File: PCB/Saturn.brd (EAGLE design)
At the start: 58.5 x 61 mm, 21 parts, among them U1A SN74AHCT125N, U2A SN74AHCT125N, U3A SN74AHCT125N, U4A SN74AHCT125N

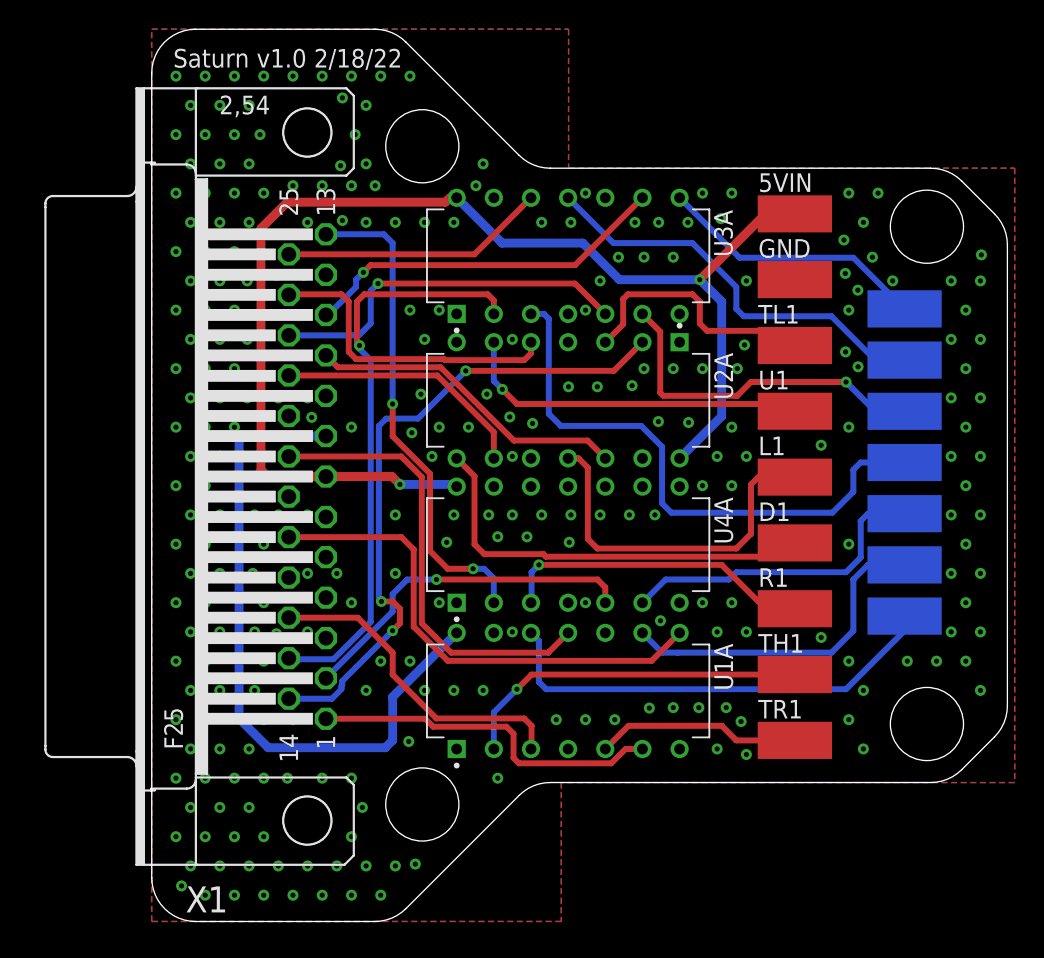
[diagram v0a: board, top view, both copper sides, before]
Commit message: PCB Updates/New Additions
All existing PCBs had silkscreen updates and NES, Virtual Boy, PSX/PS2, Nintendo 64, Saturn have been added.
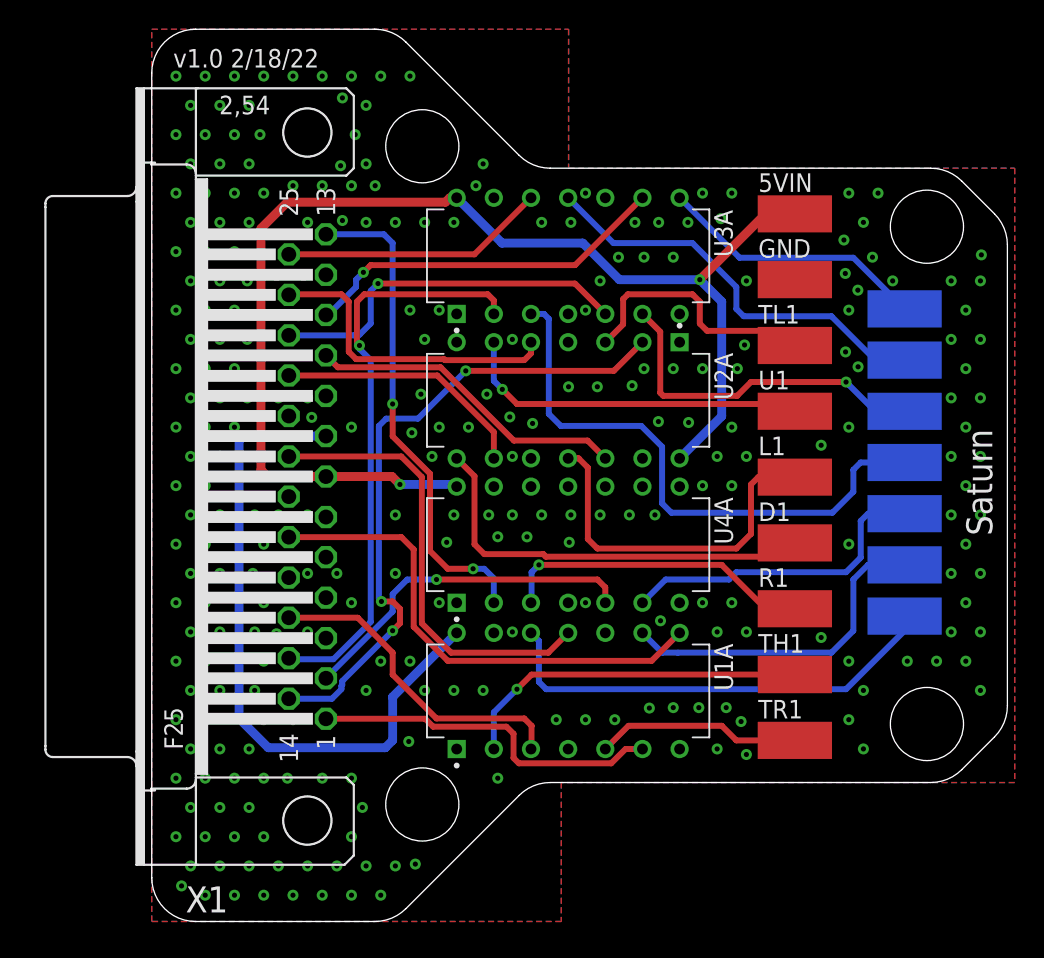
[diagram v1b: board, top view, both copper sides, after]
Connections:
- net NEEDPINID renamed IO16
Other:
- board text added: "Saturn"
- board text added: "v1.0 2/18/22"
- board text removed: "Saturn v1.0 2/18/22"
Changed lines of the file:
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@@
 <drawing>
 <settings>
-<setting alwaysvectorfont="yes"/>
+<setting alwaysvectorfont="no"/>
 <setting verticaltext="up"/>
 </settings>
@@
 <hole x="18.53" y="53.12" drill="5"/>
 <hole x="18.53" y="8.12" drill="5"/>
-<text x="1.5" y="58.5" size="1.27" layer="21">Saturn v1.0 2/18/22</text>
+<text x="1.5" y="58.5" size="1.27" layer="21">v1.0 2/18/22</text>
+<text x="57.5" y="26.5" size="1.778" layer="21" rot="R90">Saturn</text>
 </plain>
 <attributes>
@@
 <wire x1="47.5" y1="16" x2="51.5" y2="20" width="0.4064" layer="16"/>
 </signal>
-<signal name="NEEDPINID">
-<contactref element="U1A" pad="11"/>
-<contactref element="X1" pad="20"/>
-<wire x1="28.5" y1="19.851" x2="27.149" y2="18.5" width="0.4064" layer="1"/>
-<wire x1="27.149" y1="18.5" x2="20.5" y2="18.5" width="0.4064" layer="1"/>
-<wire x1="18.5" y1="20.5" x2="18.5" y2="30.5" width="0.4064" layer="1"/>
-<wire x1="18.5" y1="30.5" x2="17.0884" y2="31.9116" width="0.4064" layer="1"/>
-<wire x1="17.0884" y1="31.9116" x2="9.4" y2="31.9116" width="0.4064" layer="1"/>
-<wire x1="20.5" y1="18.5" x2="18.5" y2="20.5" width="0.4064" layer="1"/>
-</signal>
 <signal name="TL1">
 <contactref element="U2A" pad="3"/>
@@
 <wire x1="35.169" y1="23.5" x2="39.5" y2="23.5" width="0.4064" layer="16"/>
 </signal>
+<signal name="IO16">
+<contactref element="X1" pad="20"/>
+<contactref element="U1A" pad="11"/>
+<wire x1="28.5" y1="19.851" x2="27.149" y2="18.5" width="0.4064" layer="1"/>
+<wire x1="27.149" y1="18.5" x2="20.5" y2="18.5" width="0.4064" layer="1"/>
+<wire x1="18.5" y1="20.5" x2="18.5" y2="30.5" width="0.4064" layer="1"/>
+<wire x1="17.0884" y1="31.9116" x2="18.5" y2="30.5" width="0.4064" layer="1"/>
+<wire x1="20.5" y1="18.5" x2="18.5" y2="20.5" width="0.4064" layer="1"/>
+<wire x1="9.4" y1="31.9116" x2="17.0884" y2="31.9116" width="0.4064" layer="1"/>
+</signal>
 </signals>

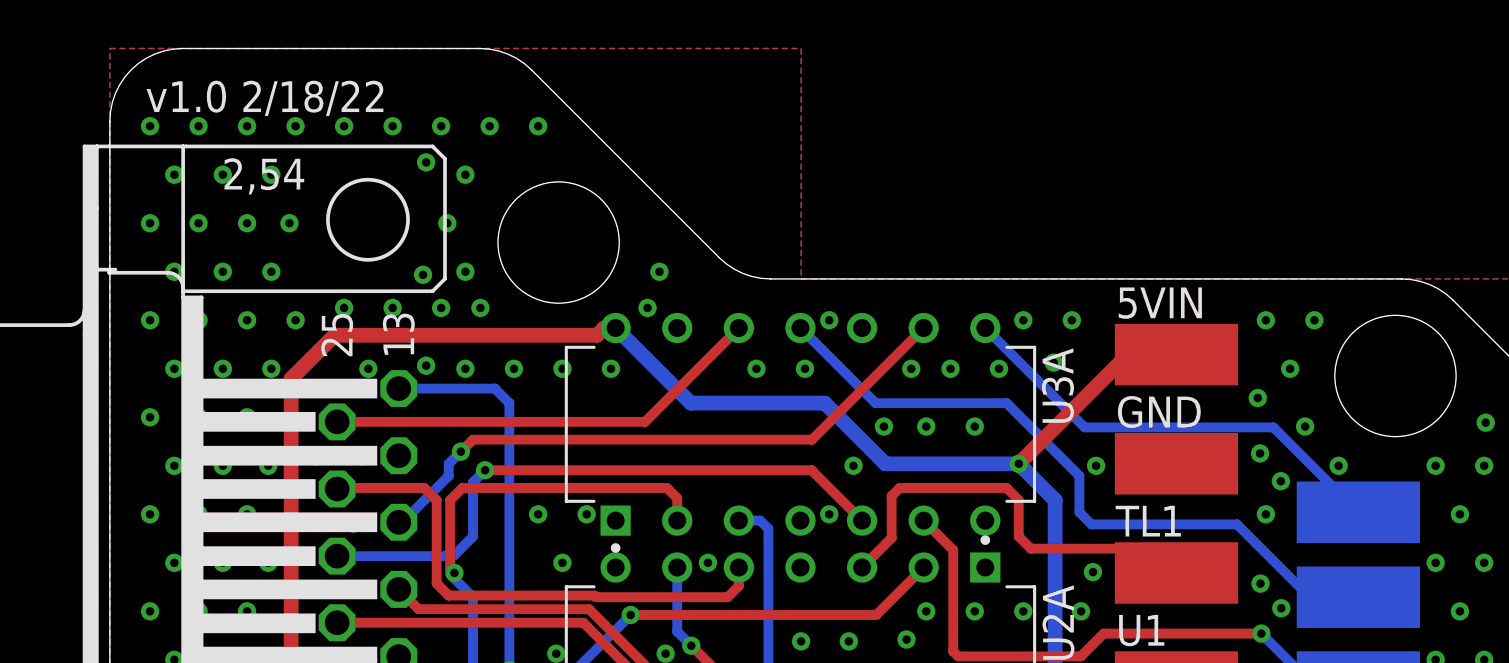
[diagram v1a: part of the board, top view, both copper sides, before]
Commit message: Datasheets, BOM Update, 3 New PCBs
Added Datasheets for the Female/Male DB25 connectors
Updated formatting on the BOM

New PCBs:
Added Nintendo 64 (Updated to 1.1, Moved VIN from 5V to 3V3)
Added Sega Saturn (Updated to 1.1, Added 5V and GND Pads on bottom for Second player pads to ease install)
Added NES

Removed PSX/PS2 and Virtual Boy as work is not complete (New branches will be made for each one)
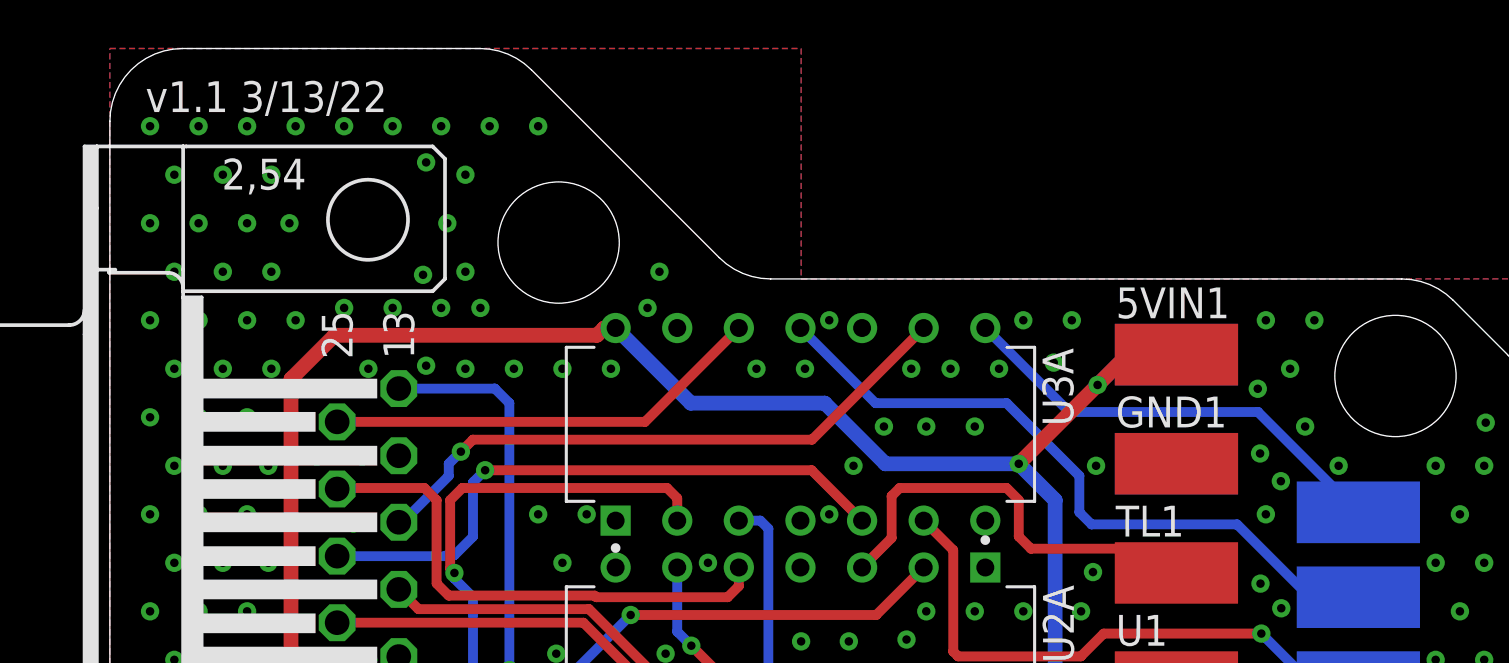
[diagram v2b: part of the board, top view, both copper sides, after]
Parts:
- removed 5VIN, GND: (no value), wirepad:SMD2,54-5,08
- added 5VIN1, 5VIN2, GND1, GND2: (no value), wirepad:SMD2,54-5,08
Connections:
- net 5VIN: now also 5VIN1.1, 5VIN2.1; no longer 5VIN.1
- net GND: now also GND1.1, GND2.1; no longer GND.1
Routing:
- net 5VIN: track 85.9 -> 89.7 mm, vias 2 -> 3
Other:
- board text added: "v1.1 3/13/22"
- board text removed: "v1.0 2/18/22"

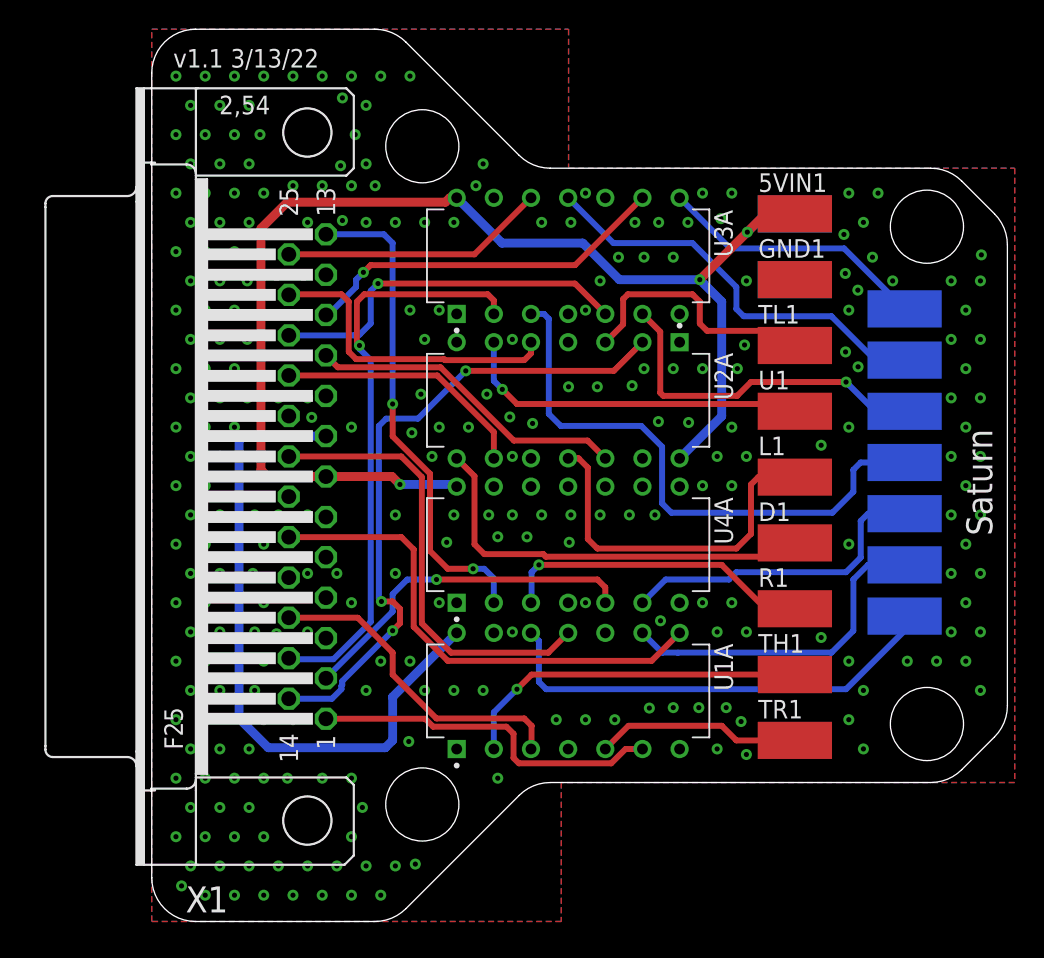
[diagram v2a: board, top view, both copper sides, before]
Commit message: PCB Update for better Housing Fit
All the PCBs were updated for better housing fitment.

Common Changes across all PCBs:
1. All Aux PCBs are now the exact same size.  (there was a .1mm-.5mm Variance previous)
2. All Aux PCBs Mounting holes are in the same location (there was a .05mm-.1mm Variance previous)
3. The DB25 has been moved 1.2mm close to the edge of the PCB for better connection when in the housing.

PCB Specific Updates:
3DO - Rename Pads (Removed trailing numbers), Flipped U2 to match U1, Moved U1 & U2 to same coordinates as other 2 Component PCBs in collection.

PCE & NES- Moved U1 & U2 to same coordinates as other 2 Component PCBs in collection.

PS2/PSX & Saturn - Added Notch on back edge of PCB for access for wires that need to attach to bottom layer of PCB.

All Gerbers have been updated.

New PCBs have been ordered for testing.
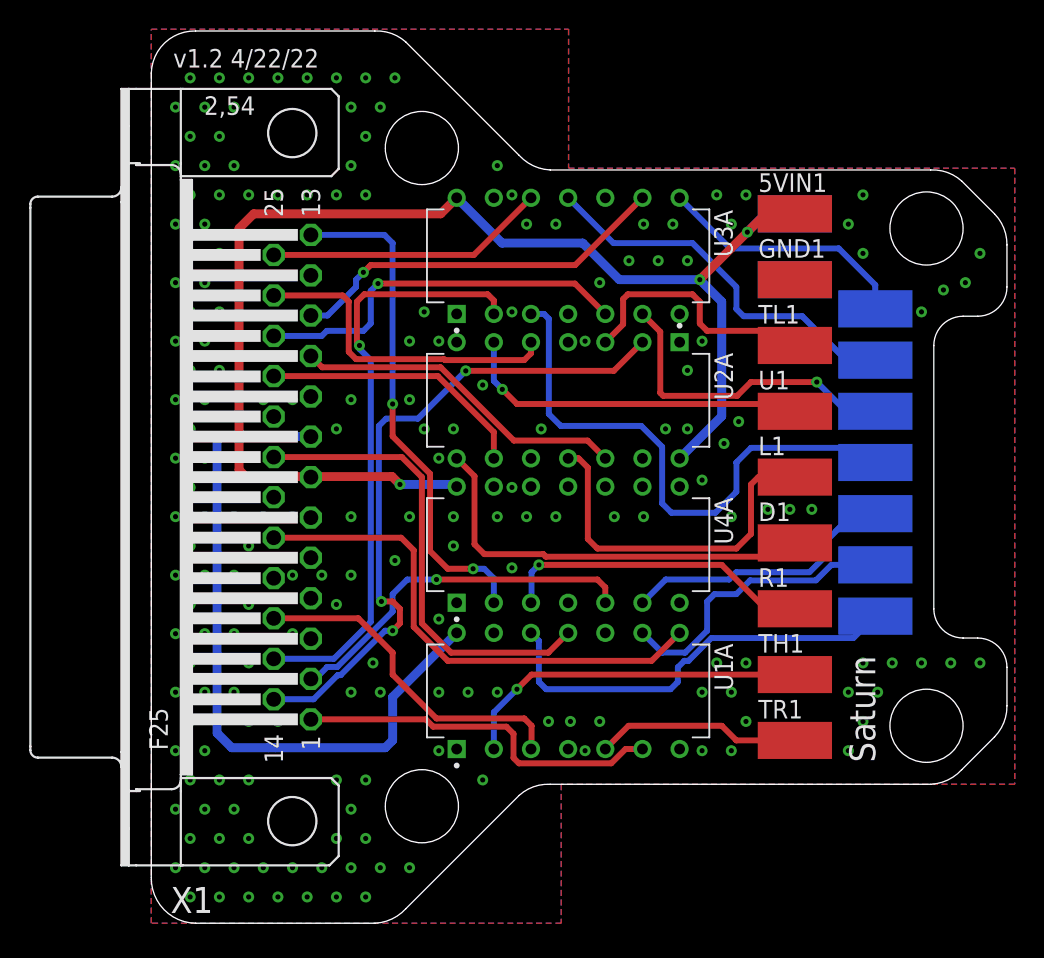
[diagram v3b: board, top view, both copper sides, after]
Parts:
- moved D2 2.00 mm to (49.5, 42.0)
- moved L2 2.00 mm to (49.5, 38.5)
- moved R2 2.00 mm to (49.5, 28.0)
- moved TH2 2.00 mm to (49.5, 24.5)
- moved TL2 2.00 mm to (49.5, 31.5)
- moved TR2 2.00 mm to (49.5, 21.0)
- moved U2 2.00 mm to (49.5, 35.0)
- moved X1 1.03 mm to (9.64, 30.5)
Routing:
- net 5VIN: track 89.7 -> 92.7 mm
- net TH2: track 23.0 -> 20.1 mm
- net R2: track 21.9 -> 19.0 mm
- net 3V3IN: track 45.8 -> 48.3 mm
- net U2: track 23.9 -> 21.9 mm
- net TR2: track 31.4 -> 29.4 mm
- net L2: track 28.5 -> 26.5 mm
- net IO25: track 23.9 -> 24.9 mm
- net IO22: track 18.2 -> 19.2 mm
- net IO21: track 25.2 -> 26.3 mm
- net IO19: track 25.3 -> 26.3 mm
- net D2: track 18.5 -> 17.5 mm
- net IO5: track 17.4 -> 18.4 mm
- net IO27: track 24.3 -> 25.3 mm
- net IO16: track 31.1 -> 32.1 mm
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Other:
- outline, holes or cut-outs redrawn
- board text added: "v1.2 4/22/22"
- board text removed: "v1.1 3/13/22"
